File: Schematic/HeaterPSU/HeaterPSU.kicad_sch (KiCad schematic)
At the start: 58 parts, among them J201 SMPS2_SEC, J202 Heater Output, J203 Heater Control, J204 MCU_Interface, J205 High voltage warning, K201 Relay_TE_OJT_SH_124DM, Q201 IRF4905, Q202 BSS138, SW201 SW_Rotary_1P5T_ALPSALPINE_SRBV, U201 TPS54302, U202 TLP185, U203 TLP185

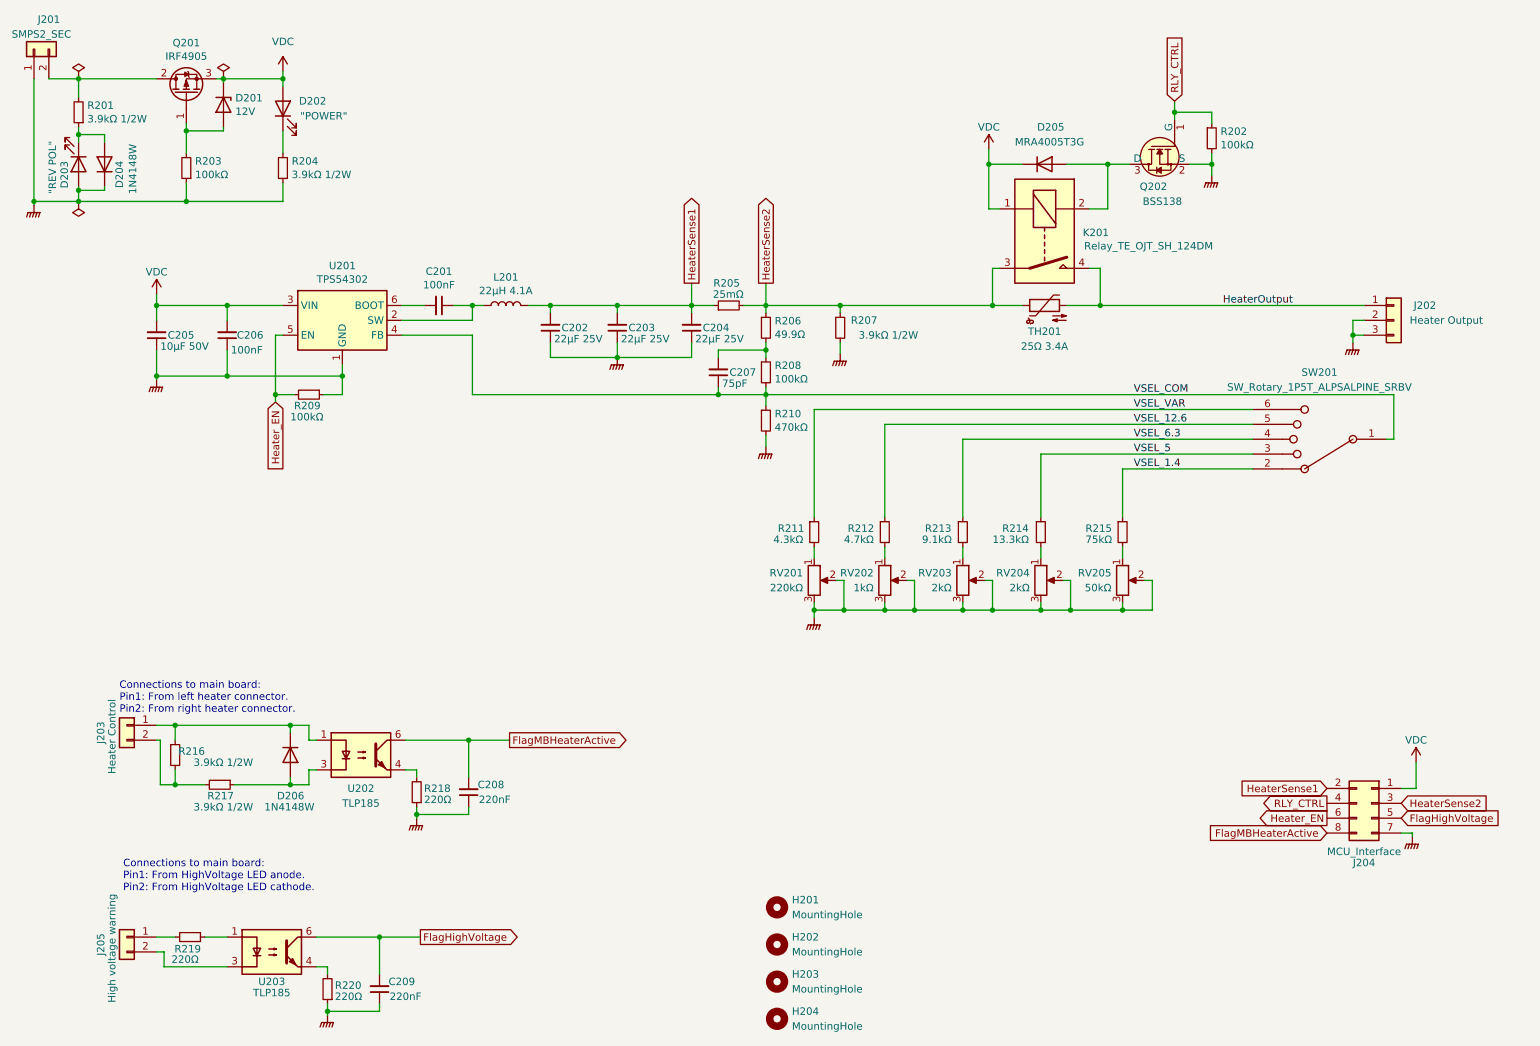
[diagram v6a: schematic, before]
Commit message: Optocouplers moved to from PSU to MCU board
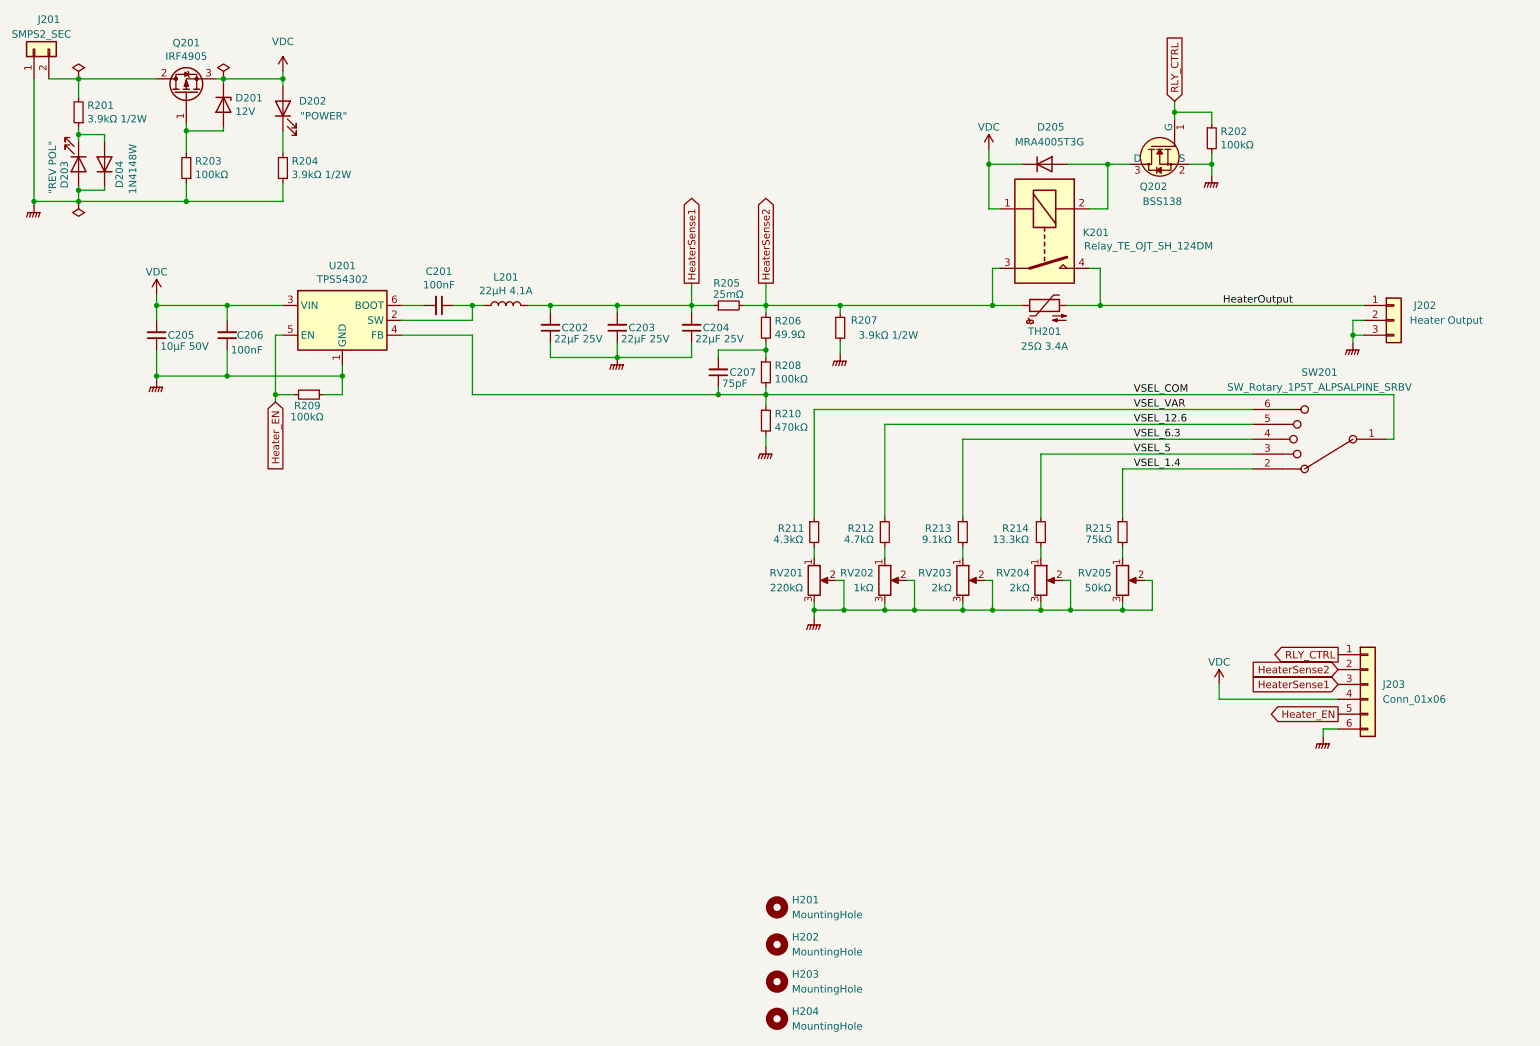
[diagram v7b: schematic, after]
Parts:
- removed C208, C209: 220nF, Capacitor_SMD:C_0805_2012Metric_Pad1.18x1.45mm_HandSolder, symbol Device:C_Small
- removed D206: 1N4148W, Diode_SMD:D_SOD-123, symbol Diode:1N4148W
- removed J203: Heater Control, myDevices:KF2510-2P, symbol Connector_Generic:Conn_01x02
- removed J204: MCU_Interface, Connector_PinSocket_2.54mm:PinSocket_2x04_P2.54mm_Vertical, symbol Connector_Generic:Conn_02x04_Odd_Even
- removed J205: High voltage warning, myDevices:KF2510-2P, symbol Connector_Generic:Conn_01x02
- removed R216, R217: 3.9kΩ 1/2W, Resistor_SMD:R_1210_3225Metric_Pad1.30x2.65mm_HandSolder, symbol Device:R_Small
- removed R218, R219, R220: 220Ω, Resistor_SMD:R_0805_2012Metric_Pad1.20x1.40mm_HandSolder, symbol Device:R_Small
- removed U202, U203: TLP185, Package_SO:SOIC-4_4.55x3.7mm_P2.54mm, symbol Isolator:TLP185
- added J203: Conn_01x06, Connector_PinSocket_2.54mm:PinSocket_1x06_P2.54mm_Vertical, symbol Connector_Generic:Conn_01x06
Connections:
- net GNDPWR: now also J203.6 (Pin_6)
- net HeaterSense1: now also J203.3 (Pin_3)
- net HeaterSense2: now also J203.2 (Pin_2)
- net Heater_EN: now also J203.5 (Pin_5)
- net RLY_CTRL: now also J203.1 (Pin_1)
- net VDC: now also J203.4 (Pin_4)
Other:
- note removed: "Connections to main board: Pin1: From HighVoltage LED anode. Pin2: From HighVoltage LED cathode."
- note removed: "Connections to main board: Pin1: From left heater connector. Pin2: From right heater connector."

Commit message: Swapped IO pins
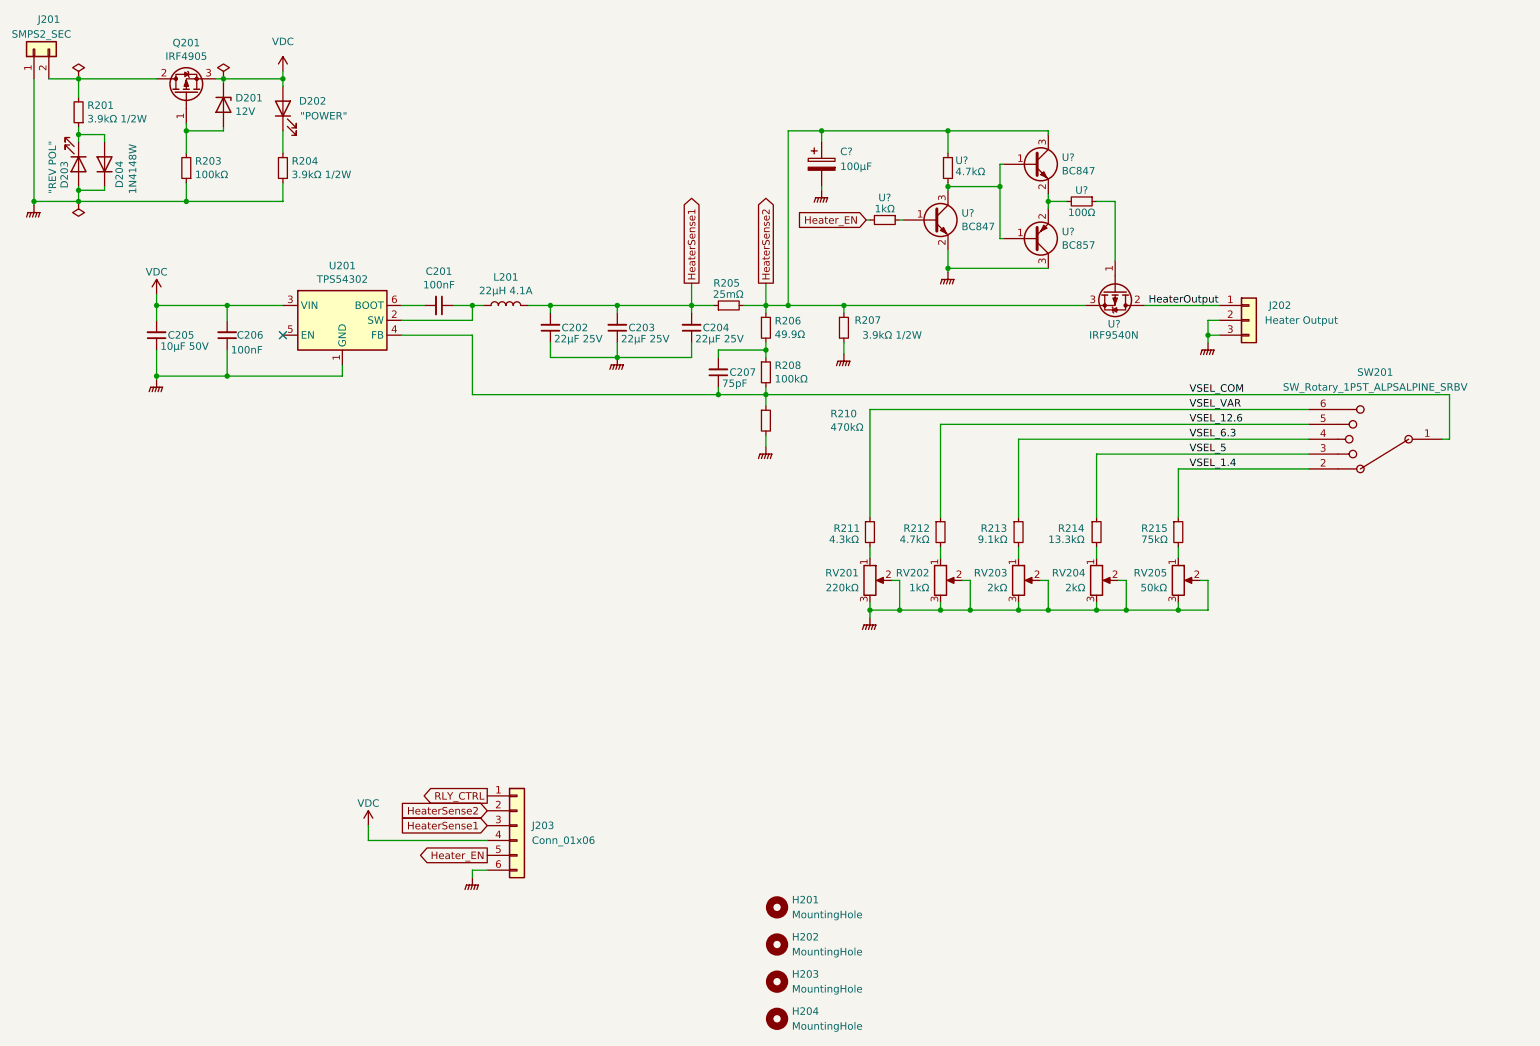
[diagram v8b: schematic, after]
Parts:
- removed D205: MRA4005T3G, Diode_SMD:D_SMA, symbol Diode:MRA4005T3G
- removed K201: Relay_TE_OJT_SH_124DM, myDevices:Relay_TE_OJT_SH_124, symbol myDevices:Relay_TE_OJT_SH_124DM
- removed Q202: BSS138, digikey-footprints:SOT-23-3, symbol dk_Transistors-FETs-MOSFETs-Single:BSS138
- removed R202, R209: 100kΩ, Resistor_SMD:R_0805_2012Metric_Pad1.20x1.40mm_HandSolder, symbol Device:R_Small
- removed TH201: 25Ω 3.4A, myDevices:RV_Disc_D15.5mm_W4.5mm_P7.5mm, symbol Device:Thermistor_NTC
- added C?: 100µF, symbol Device:C_Polarized
- added U?: 1kΩ, Resistor_SMD:R_0805_2012Metric_Pad1.15x1.40mm_HandSolder, symbol Device:R_Small
- added U? (x2): BC847, Package_TO_SOT_SMD:SOT-23, symbol Transistor_BJT:BC847
- added U?: 4.7kΩ, Resistor_SMD:R_0805_2012Metric_Pad1.15x1.40mm_HandSolder, symbol Device:R_Small
- added U?: IRF9540N, Package_TO_SOT_SMD:TO-263-2, symbol Transistor_FET:IRF9540N
- added U?: BC857, Package_TO_SOT_SMD:SOT-23, symbol Transistor_BJT:BC857
- added U?: 100Ω, Resistor_SMD:R_0805_2012Metric_Pad1.15x1.40mm_HandSolder, symbol Device:R_Small
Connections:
- net GNDPWR: now also C?.2, U?.2 (E), U?.3 (C)
- net HeaterOutput: now also U?.2 (D)
- net HeaterSense2: now also C?.1, U?.1, U?.3 (C), U?.3 (S)
- net Heater_EN: now also U?.2; no longer U201.5 (EN)
- new net: U?.1, U?.1 (B)
- new net: U?.1 (B), U?.1 (B), U?.2, U?.3 (C)
- new net: U?.2, U?.2 (E), U?.2 (E)
- new net: U?.1, U?.1 (G)
- no-connect marks 0 -> 1
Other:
- moved on the sheet: J202, J203, R207, R211, R212, R213, R214, R215, RV201, RV202, RV203, RV204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
